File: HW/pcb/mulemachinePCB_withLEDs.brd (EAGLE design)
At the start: 68.6 x 54.6 mm, 33 parts, among them IC1 LD117AV50, IC2 MEGA8-P, J1 DCJ0202, Q1 16Mhz

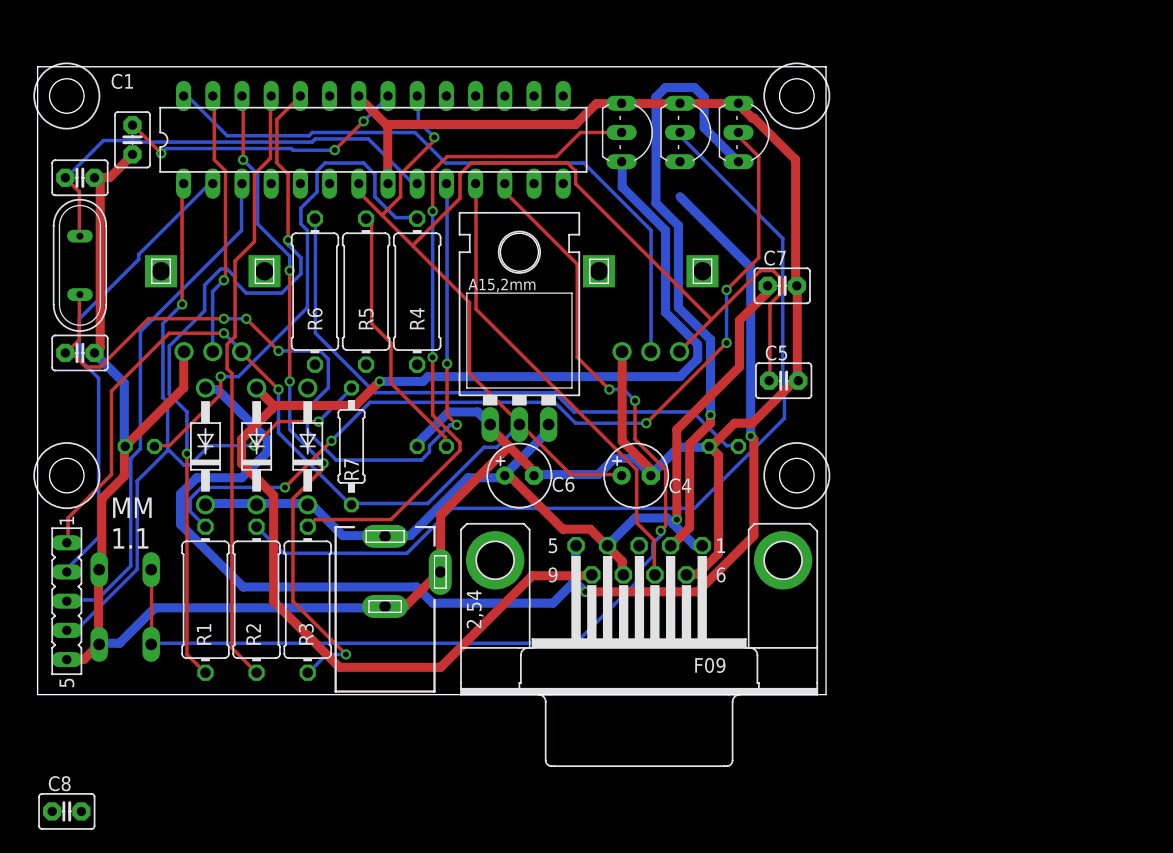
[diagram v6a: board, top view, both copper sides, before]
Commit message: rotated MCU to allow for better routing. added top and bottom layer ground planes with vias connecting them.
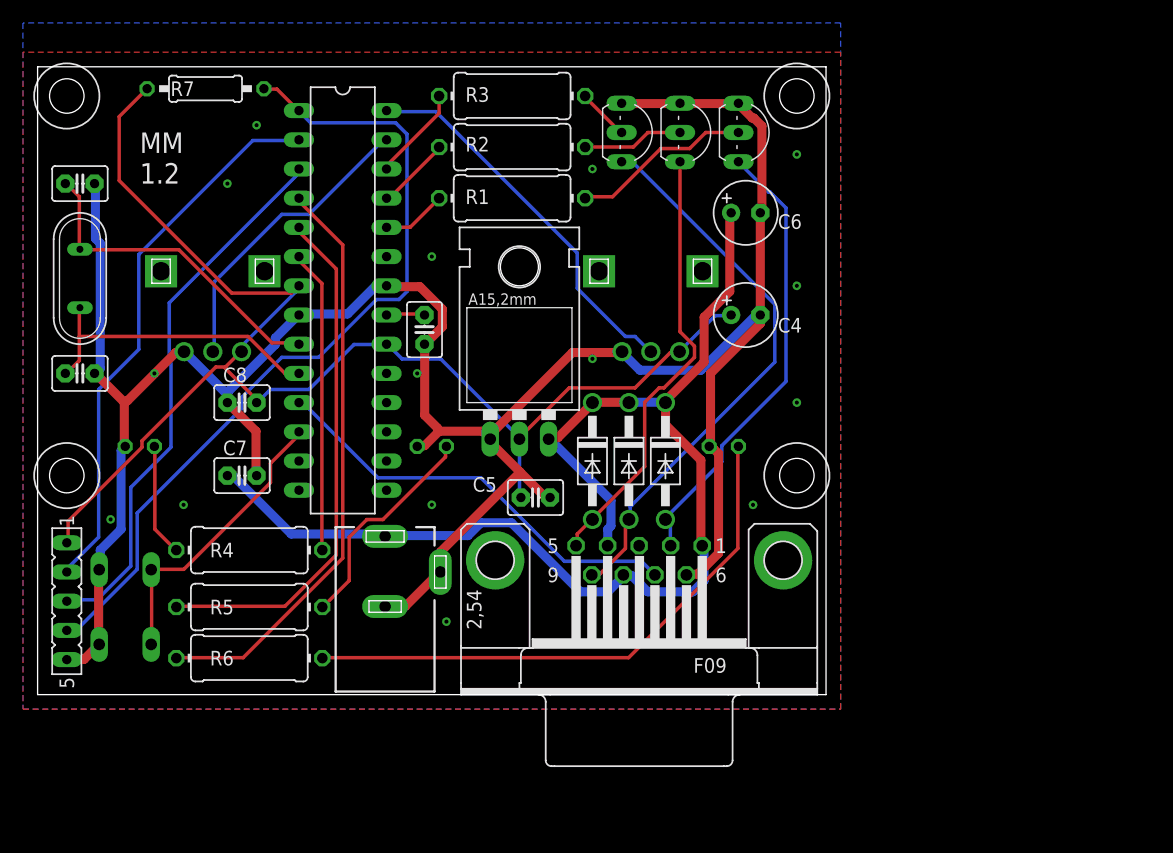
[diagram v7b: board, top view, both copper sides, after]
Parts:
- moved C7 49.8 mm to (17.8, 19.1)
- moved R3 47.3 mm to (41.3, 52.1), turned to 0 degrees
- moved R2 45.2 mm to (41.3, 47.6), turned to 0 degrees
- moved R1 43.9 mm to (41.3, 43.2), turned to 0 degrees
- moved C8 38.7 mm to (17.8, 25.4)
- moved D2 33.7 mm to (48.3, 20.3), turned to 270 degrees
- moved R7 33.6 mm to (14.6, 52.7), turned to 0 degrees
- moved D3 32.4 mm to (51.4, 20.3), turned to 270 degrees
- moved R6 32.4 mm to (18.4, 3.17), turned to 0 degrees
- moved D1 31.1 mm to (54.6, 20.3), turned to 270 degrees
- moved C1 30.3 mm to (33.7, 31.8)
- moved C6 30.2 mm to (61.6, 41.9)
- moved R5 29.3 mm to (18.4, 7.62), turned to 0 degrees
- moved R4 26.8 mm to (18.4, 12.6), turned to 180 degrees
- moved C5 23.9 mm to (43.3, 17.1)
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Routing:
- net PUMP_GB_VCC: track 111.2 -> 38.5 mm, vias 2 -> 0
- net N$6: track 80.4 -> 8.78 mm
- net MANUALOVERRIDE: track 93.3 -> 25.5 mm, vias 3 -> 0
- net PUMP_LIME_VCC: track 113.2 -> 49.0 mm, vias 1 -> 0
- net N$10: track 77.0 -> 15.8 mm, vias 5 -> 0
- net PUMP_VODKA: track 64.1 -> 5.63 mm, vias 2 -> 0
- net N$5: track 59.1 -> 4.54 mm, vias 2 -> 0
- net LED_GREEN: track 0.00 -> 51.0 mm
- net 5V: track 171.4 -> 121.0 mm, vias 3 -> 0
- net PUMP_LIME: track 58.4 -> 8.24 mm, vias 5 -> 0
- net N$11: track 76.4 -> 26.7 mm, vias 5 -> 0
- net PUMP_GB: track 52.7 -> 6.50 mm
- net LED_YELLOW: track 0.00 -> 45.6 mm
- net ORANGE: track 44.1 -> 9.83 mm, vias 1 -> 0
- net LED_ORANGE: track 0.00 -> 26.4 mm
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- added copper zone on layer 1, net GND
- added copper zone on layer 16, net GND
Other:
- board text added: "MM 1.2"
- board text removed: "MM 1.1"

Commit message: adjusted net classes so that pump VCCs lines were also considered power traces (wider). rerouted and adjusted GND planes
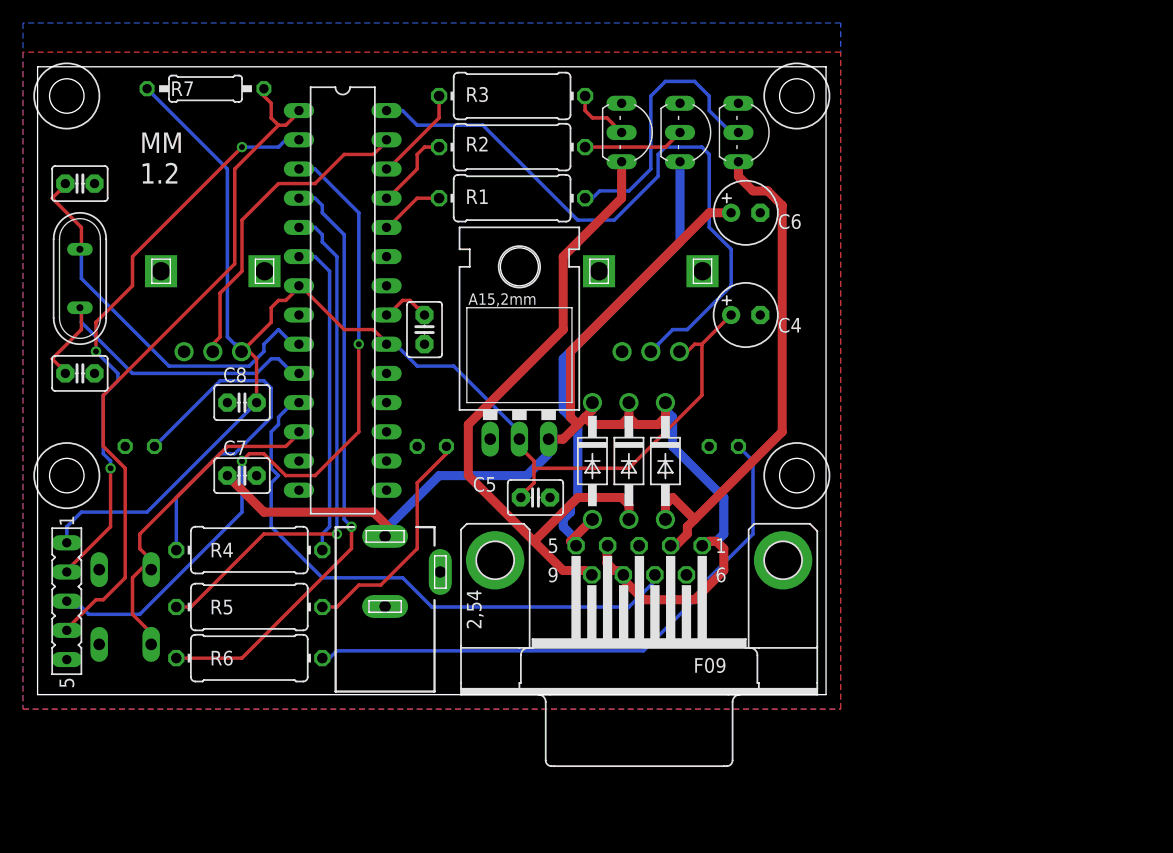
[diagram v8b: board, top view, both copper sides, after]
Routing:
- net GND: track 220.1 -> 0.00 mm, vias 15 -> 0
- net SOURRPOT: track 33.5 -> 58.8 mm
- net ORANGE: track 9.83 -> 31.1 mm
- net TX: track 47.6 -> 62.8 mm, vias 0 -> 2
- net CUPSENSOR: track 37.2 -> 50.6 mm
- net RESET: track 73.0 -> 59.8 mm
- net PUMP_LIME_VCC: track 49.0 -> 58.5 mm
- net N$10: track 15.8 -> 23.8 mm
- net N$12: track 28.7 -> 34.9 mm
- net VCC: track 107.5 -> 113.0 mm
- net PUMP_VODKA_VCC: track 39.7 -> 45.1 mm
- net MANUALOVERRIDE: track 25.5 -> 30.7 mm
- net N$11: track 26.7 -> 31.1 mm
- net PUMP_GB_VCC: track 38.5 -> 42.5 mm
- net RX: track 48.3 -> 50.6 mm, vias 0 -> 3
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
